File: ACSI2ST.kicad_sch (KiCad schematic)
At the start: 56 parts, among them J10 RESET, J11 FLASH, J12 ID_SHIFT, J13 STRICT, J14 UART, P1 IDC20, U1 XC6206PxxxMR, U2 STM32F103C8Tx, X1 32.768KHz, X2 8MHz

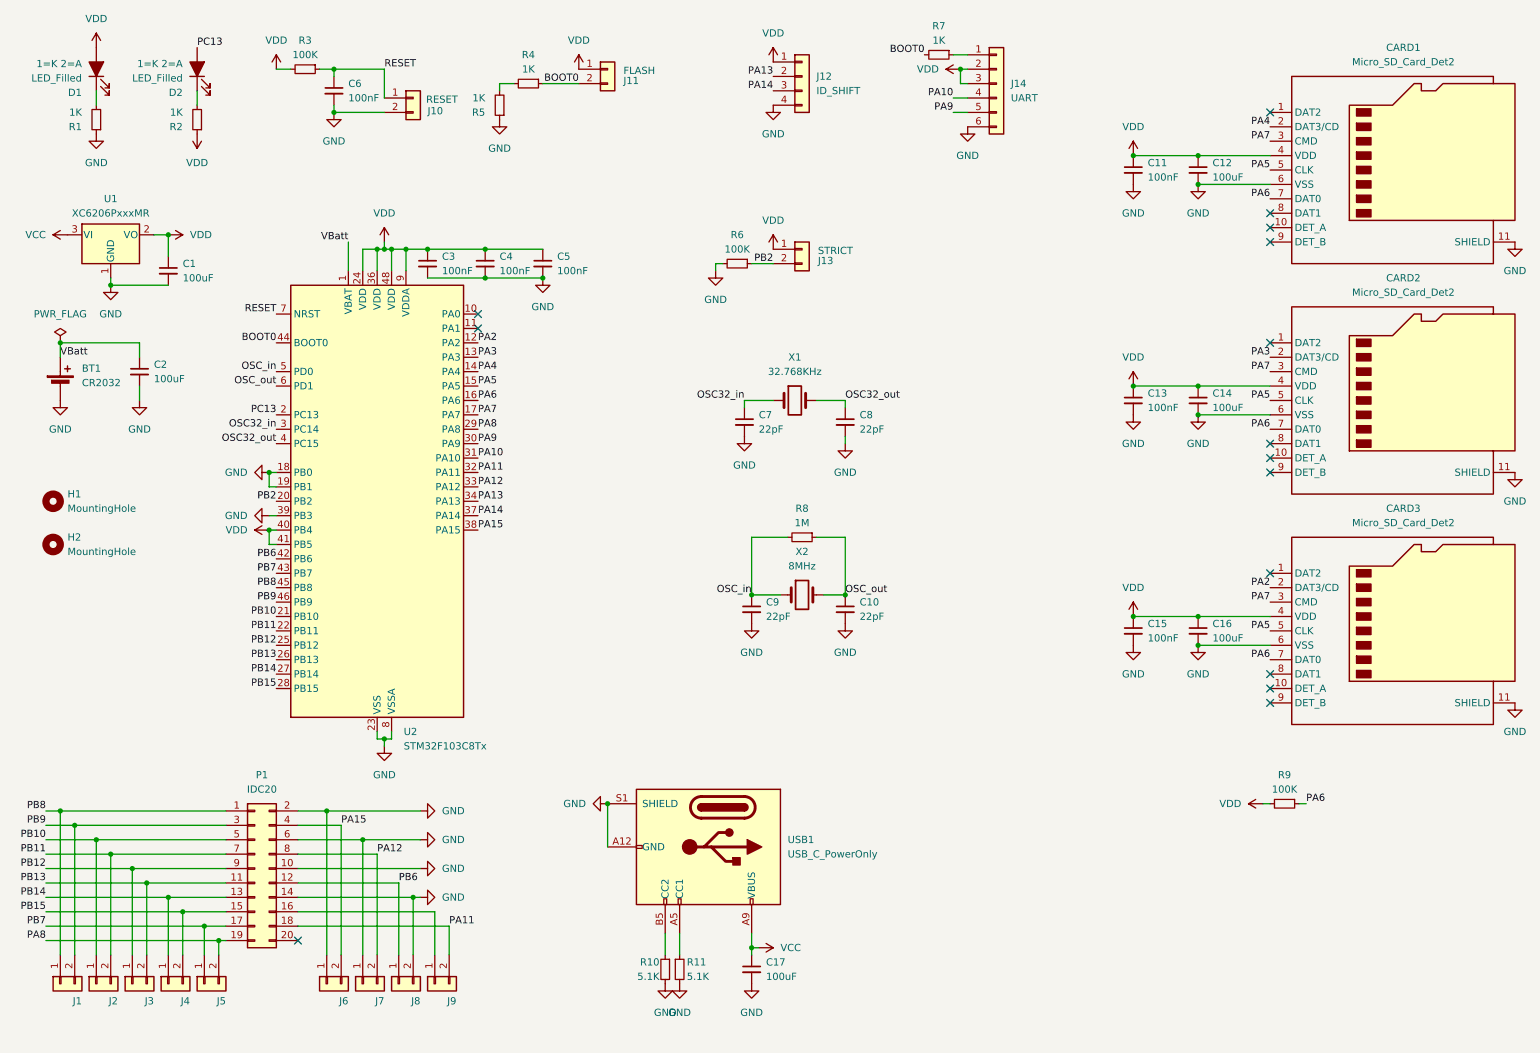
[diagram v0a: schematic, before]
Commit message: use single pins for db19
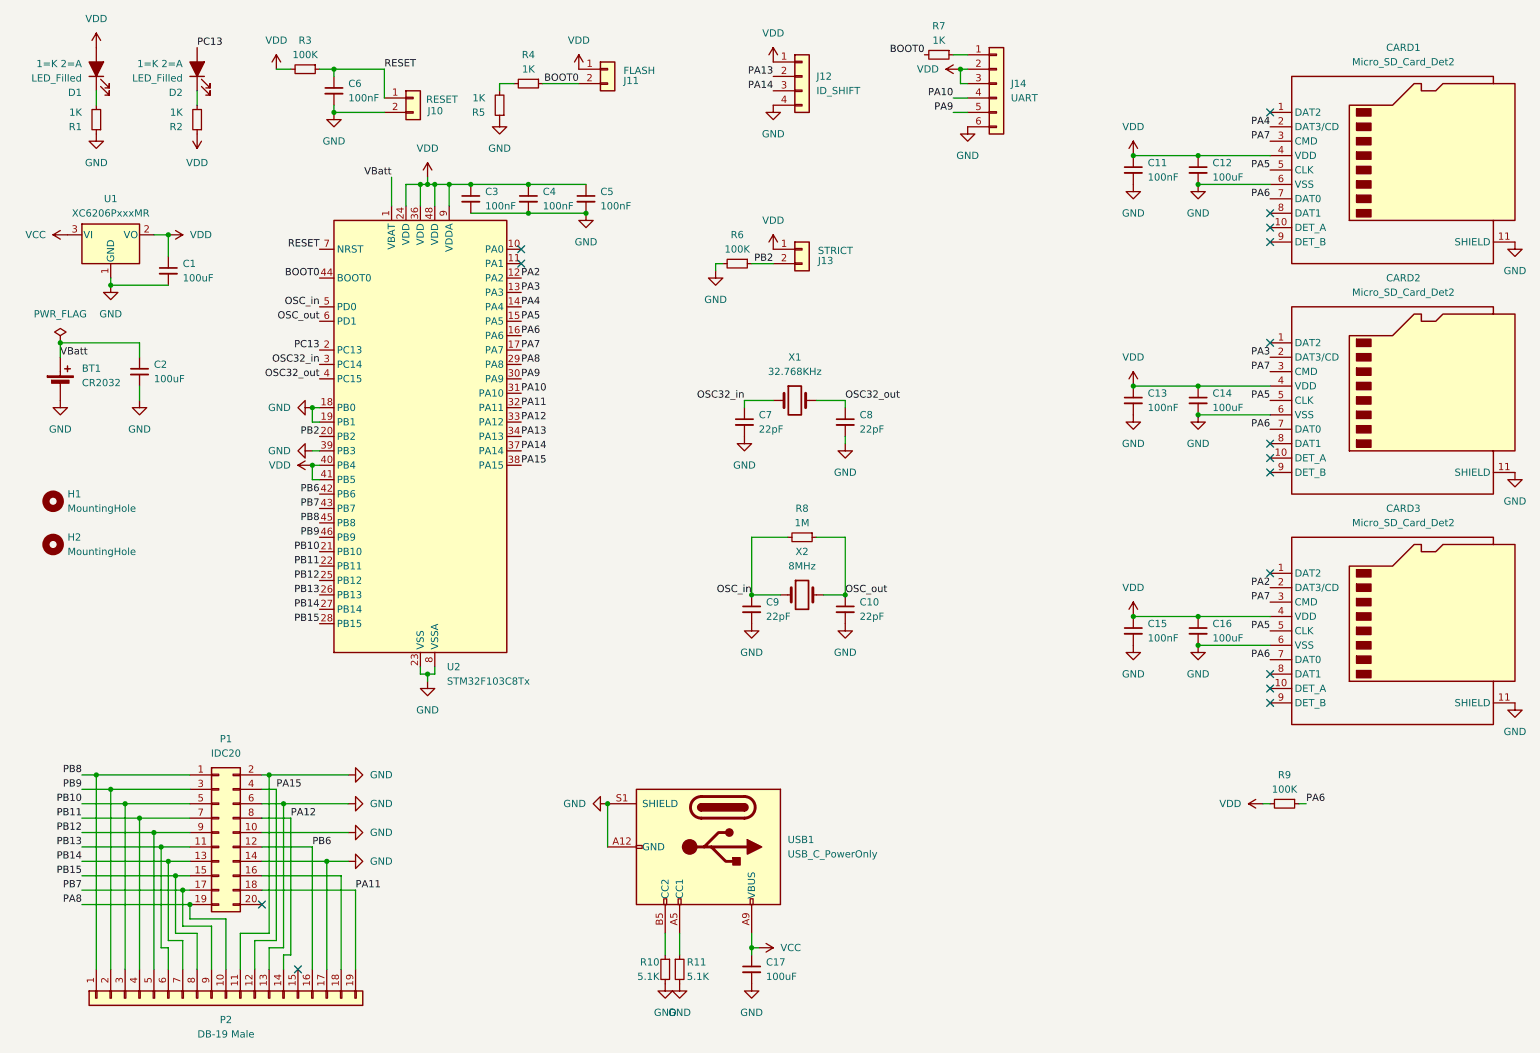
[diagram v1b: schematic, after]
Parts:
- removed J1, J2, J3, J4, J5, J6, J7, J8, J9: ~, Connector_PinHeader_2.54mm:PinHeader_1x02_P2.54mm_Vertical, symbol Connector_Generic:Conn_01x02
- added P2: DB-19 Male, ACSI2ST:DSUB-19_Pins_Vertical, symbol Connector_Generic:Conn_01x19
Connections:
- net GND: now also P2.11 (Pin_11), P2.13 (Pin_13), P2.17 (Pin_17)
- net PA11: now also P2.19 (Pin_19)
- net PA12: now also P2.14 (Pin_14)
- net PA15: now also P2.12 (Pin_12)
- net PA8: now also P2.10 (Pin_10)
- net PB10: now also P2.3 (Pin_3)
- net PB11: now also P2.4 (Pin_4)
- net PB12: now also P2.5 (Pin_5)
- net PB13: now also P2.6 (Pin_6)
- net PB14: now also P2.7 (Pin_7)
- net PB15: now also P2.8 (Pin_8)
- net PB6: now also P2.16 (Pin_16)
- net PB7: now also P2.9 (Pin_9)
- net PB8: now also P2.1 (Pin_1)
- net PB9: now also P2.2 (Pin_2)
- net at P1.16 (Pin_16): now also P2.18 (Pin_18)
- no-connect marks 15 -> 16
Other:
- moved on the sheet: C3, C4, C5, P1, U2

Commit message: Final update in preparation for fabrication
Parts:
- added J1: 5V PWR, Connector_PinHeader_2.54mm:PinHeader_1x02_P2.54mm_Vertical, symbol Connector_Generic:Conn_01x02
- H1, H2: footprint MountingHole:MountingHole_3.2mm_M3 -> MountingHole:MountingHole_2.5mm
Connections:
- net GND: now also J1.1 (Pin_1)
- net VCC: now also J1.2 (Pin_2)
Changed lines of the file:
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@@
 	)
 	(symbol
+		(lib_id "Connector_Generic:Conn_01x02")
+		(at 27.94 132.08 270)
+		(unit 1)
+		(exclude_from_sim no)
+		(in_bom yes)
+		(on_board yes)
+		(dnp yes)
+		(fields_autoplaced yes)
+		(property "Reference" "J1"
+			(at 30.48 130.8099 90)
+			(effects
+				(font
+					(size 1.27 1.27)
+				)
+				(justify left)
+			)
+		)
+		(property "Value" "5V PWR"
+			(at 30.48 133.3499 90)
+			(effects
+				(font
+					(size 1.27 1.27)
+				)
+				(justify left)
+			)
+		)
+		(property "Footprint" "Connector_PinHeader_2.54mm:PinHeader_1x02_P2.54mm_Vertical"
+			(at 27.94 132.08 0)
+			(effects
+				(font
+					(size 1.27 1.27)
+				)
+				(hide yes)
+			)
+		)
+		(property "Datasheet" "~"
+			(at 27.94 132.08 0)
+			(effects
+				(font
+					(size 1.27 1.27)
+				)
+				(hide yes)
+			)
+		)
+		(property "Description" "Generic connector, single row, 01x02, script generated (kicad-library-utils/schlib/autogen/connector/)"
+			(at 27.94 132.08 0)
+			(effects
+				(font
+					(size 1.27 1.27)
+				)
+				(hide yes)
+			)
+		)
+		(pin "2"
+		)
+		(pin "1"
+		)
+		(instances
+			(project ""
+				(path "/8604a45c-e5b6-4ceb-bc1a-e86e00a60426"
+					(reference "J1")
+					(unit 1)
+				)
+			)
+		)
+	)
+	(symbol
 		(lib_id "Device:Crystal")
 		(at 151.13 118.11 0)
@@
 			)
 		)
-		(property "Footprint" "MountingHole:MountingHole_3.2mm_M3"
+		(property "Footprint" "MountingHole:MountingHole_2.5mm"
 			(at 19.05 109.22 0)
 			(effects
@@
 	)
 	(symbol
+		(lib_id "power:VCC")
+		(at 25.4 127 0)
+		(mirror y)
+		(unit 1)
+		(exclude_from_sim no)
+		(in_bom yes)
+		(on_board yes)
+		(dnp no)
+		(fields_autoplaced yes)
+		(property "Reference" "#PWR033"
+			(at 25.4 130.81 0)
+			(effects
+				(font
+					(size 1.27 1.27)
+				)
+				(hide yes)
+			)
+		)
+		(property "Value" "VCC"
+			(at 25.4 121.92 0)
+			(effects
+				(font
+					(size 1.27 1.27)
+				)
+			)
+		)
+		(property "Footprint" ""
+			(at 25.4 127 0)
+			(effects
+				(font
+					(size 1.27 1.27)
+				)
+				(hide yes)
+			)
+		)
+		(property "Datasheet" ""
+			(at 25.4 127 0)
+			(effects
+				(font
+					(size 1.27 1.27)
+				)
+				(hide yes)
+			)
+		)
+		(property "Description" "Power symbol creates a global label with name \"VCC\""
+			(at 25.4 127 0)
+			(effects
+				(font
+					(size 1.27 1.27)
+				)
+				(hide yes)
+			)
+		)
+		(pin "1"
+		)
+		(instances
+			(project "ACSI2ST"
+				(path "/8604a45c-e5b6-4ceb-bc1a-e86e00a60426"
+					(reference "#PWR033")
+					(unit 1)
+				)
+			)
+		)
+	)
+	(symbol
 		(lib_id "Mechanical:MountingHole")
 		(at 19.05 101.6 0)
@@
 			)
 		)
-		(property "Footprint" "MountingHole:MountingHole_3.2mm_M3"
+		(property "Footprint" "MountingHole:MountingHole_2.5mm"
 			(at 19.05 101.6 0)
 			(effects
@@
 					(unit 1)
 				)
+			)
+		)
+	)
+	(symbol
+		(lib_id "power:GND")
+		(at 27.94 127 0)
+		(mirror x)
+		(unit 1)
+		(exclude_from_sim no)
+		(in_bom yes)
+		(on_board yes)
+		(dnp no)
+		(fields_autoplaced yes)
+		(property "Reference" "#PWR052"
+			(at 27.94 120.65 0)
+			(effects
+				(font
+					(size 1.27 1.27)
+				)
+				(hide yes)
+			)
+		)
+		(property "Value" "GND"
+			(at 27.94 121.92 0)
+			(effects
+				(font
+					(size 1.27 1.27)
+				)
+			)
+		)
+		(property "Footprint" ""
+			(at 27.94 127 0)
+			(effects
+				(font
+					(size 1.27 1.27)
+				)
+				(hide yes)
+			)
+		)
+		(property "Datasheet" ""
+			(at 27.94 127 0)
+			(effects
+				(font
+					(size 1.27 1.27)
+				)
+				(hide yes)
+			)
+		)
+		(property "Description" "Power symbol creates a global label with name \"GND\" , ground"
+			(at 27.94 127 0)
+			(effects
+				(font
+					(size 1.27 1.27)
+				)
+				(hide yes)
+			)
+		)
+		(pin "1"
+		)
+		(instances
+			(project "ACSI2ST"
+				(path "/8604a45c-e5b6-4ceb-bc1a-e86e00a60426"
+					(reference "#PWR052")
+					(unit 1)
+				)

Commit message: tidy up
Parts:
- BT1: DigiKey (none) -> 36-1060CT-ND; LCSC (none) -> C238069
- C1, C12, C14, C16, C17, C2: LCSC (none) -> C15008
- C10, C7, C8, C9: LCSC (none) -> C1653
- C11, C13, C15, C3, C4, C5, C6: LCSC (none) -> C66501
- CARD1, CARD2, CARD3: LCSC (none) -> C597972
- D1, D2: LCSC (none) -> C84256
- H1, H2: now not fitted
- J10, J11, J13: LCSC (none) -> C124375
- J12: LCSC (none) -> C124378
- J14: LCSC (none) -> C40877
- P1: LCSC (none) -> C3405
- R1, R2, R4, R5, R7: LCSC (none) -> C2074292
- R10, R11: LCSC (none) -> C1728901
- R3, R6, R9: LCSC (none) -> C2087858
- R8: LCSC (none) -> C2073548
- U1: LCSC (none) -> C5446
- U2: value STM32F103C8Tx -> STM32F103C8T6; LCSC (none) -> C8734
- USB1: LCSC (none) -> C22383811
- X1: LCSC (none) -> C32346
- X2: LCSC (none) -> C115962
